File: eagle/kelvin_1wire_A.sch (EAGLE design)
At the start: 46 parts, among them IC1 PIC18F2580, IC3 MCP2551SN, IC4 LM2575S, J1 OSTTE-12, J2 A00-108-220-450, Q1 10 MHz

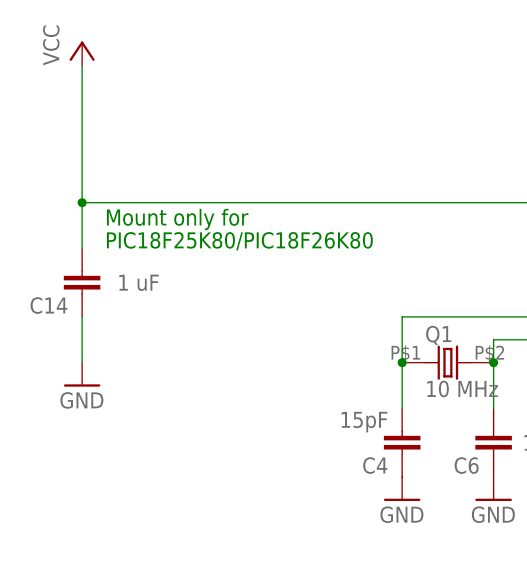
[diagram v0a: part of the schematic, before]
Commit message: Changed value of C14 to 10uF
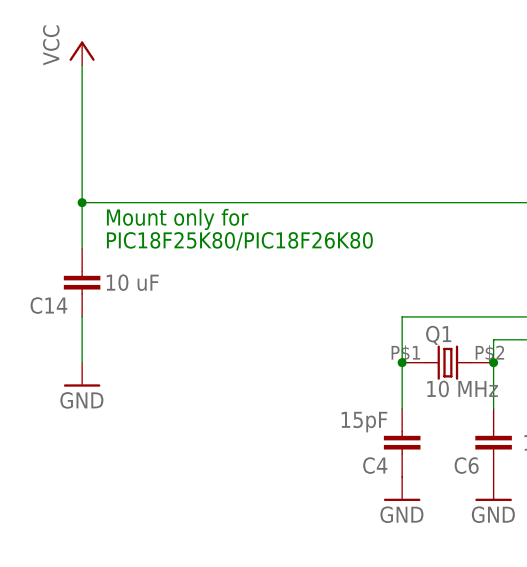
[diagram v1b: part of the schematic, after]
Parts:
- C14: value 1 uF -> 10 uF
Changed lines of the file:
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@@
 <part name="C13" library="rcl" deviceset="C-EU" device="C0805" value="10uF"/>
 <part name="GND31" library="SUPPLY1" deviceset="GND" device=""/>
-<part name="C14" library="rcl" deviceset="C-EU" device="C0805" value="1 uF"/>
+<part name="C14" library="rcl" deviceset="C-EU" device="C0805" value="10 uF"/>
 <part name="GND32" library="SUPPLY1" deviceset="GND" device=""/>
 <part name="R17" library="rcl" deviceset="R-EU_" device="R0805" value="120"/>
